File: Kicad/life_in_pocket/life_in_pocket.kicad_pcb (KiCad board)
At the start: 2 copper layers, 115.7 x 79.1 mm, 57 parts, among them J2 USB_C_Receptacle_USB2.0_16P, Q1 QM6015D, SW1 SW_SPST, SW2 Switch, SW3 Switch, SW4 Switch, SW5 Switch, U1 ESP32-S3-WROOM-1, U2 Adafruit I2S 3W Class D Ampli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, U3 MicroSd breakout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

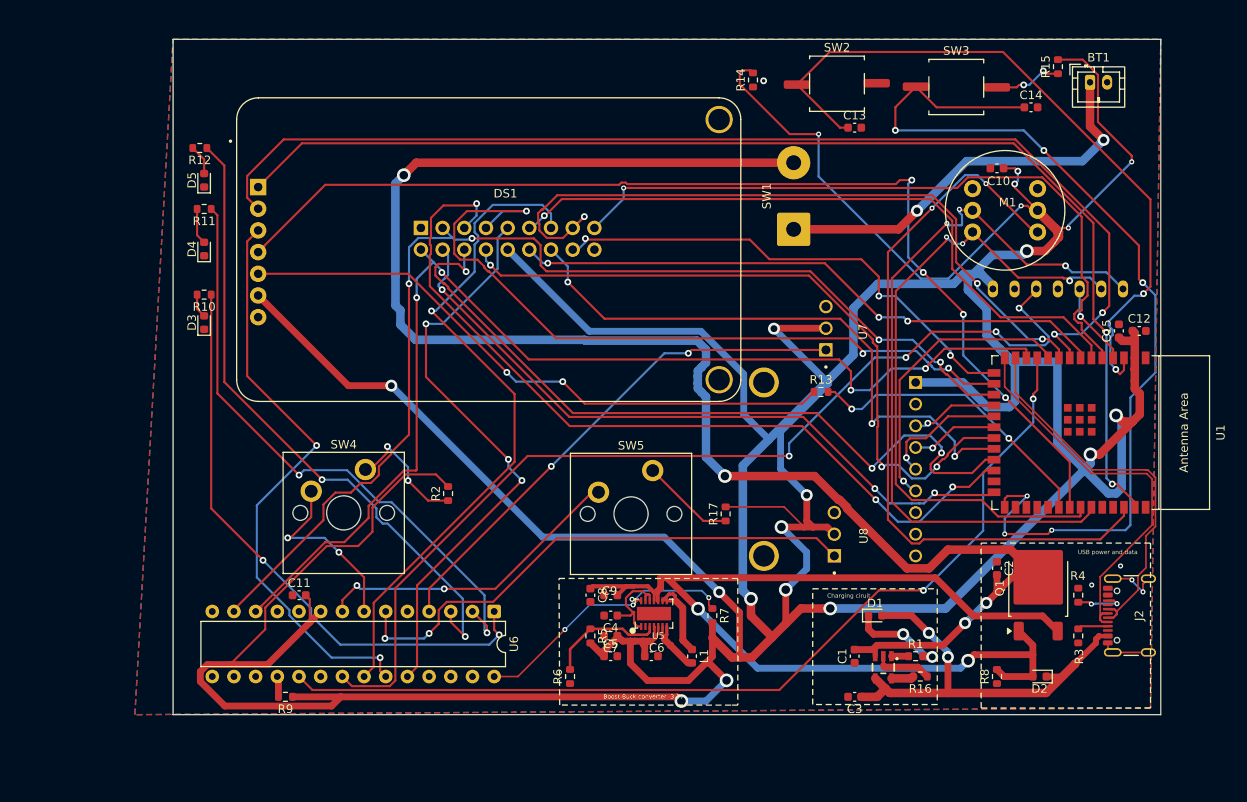
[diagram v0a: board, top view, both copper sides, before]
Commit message: Finished rerouting- all critical errors resolved
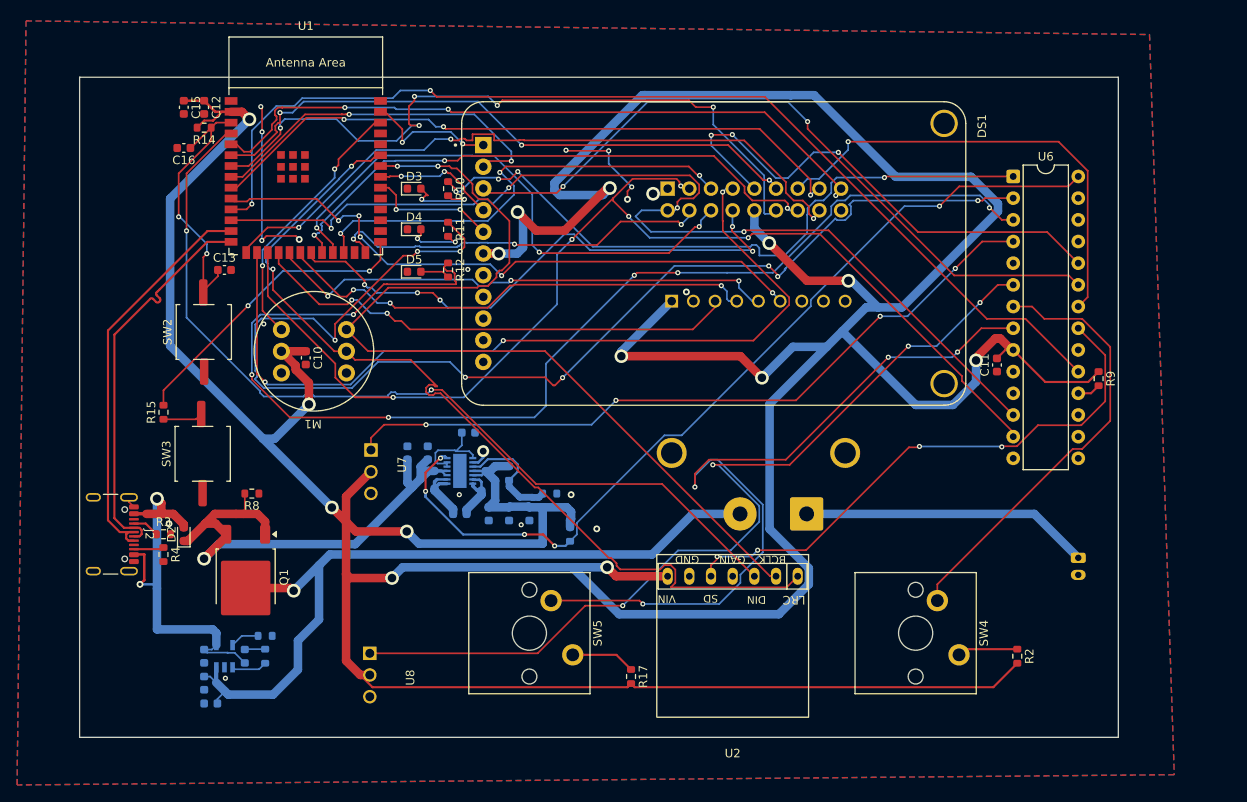
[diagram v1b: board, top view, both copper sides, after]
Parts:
- removed C14: 0.1uF, Capacitor_SMD:C_0603_1608Metric
- removed R13: 33, Resistor_SMD:R_0603_1608Metric
- added C16: 1.0uF, Capacitor_SMD:C_0603_1608Metric, F.Cu at (97.6, 52.4)
- BT1, C1, C2, C3, C4, C5, C6, C7, C8, C9, D1, L1, R1, R16, R5, R6, R7, SW1, U4, U5: moved to B.Cu
- R15: value 10k -> 100
- U2: moved to F.Cu
- moved J2 121.8 mm to (88.1, 97.6), turned to -90 degrees
- moved C12 112.6 mm to (100.0, 47.6), turned to -90 degrees
- moved C15 112.6 mm to (97.6, 47.6), turned to -90 degrees
- moved R15 112.3 mm to (95.2, 83.3)
- moved R3 107.8 mm to (95.2, 97.6), turned to 0 degrees
- moved R4 107.3 mm to (95.2, 100.0), turned to -90 degrees
- moved R9 102.3 mm to (204.8, 79.4), turned to -90 degrees
- moved D2 101.6 mm to (97.6, 97.6), turned to 90 degrees
- moved SW3 98.2 mm to (99.8, 88.2), turned to -90 degrees
- moved U1 95.2 mm to (111.9, 55.1), turned to 0 degrees
- moved C2 93.4 mm to (100.8, 117.5), turned to 0 degrees
- moved Q1 92.8 mm to (104.9, 102.7), turned to -90 degrees
- moved R8 89.9 mm to (105.6, 92.9), turned to 180 degrees
- moved C11 86.1 mm to (192.9, 77.8), turned to 90 degrees
- moved C10 84.0 mm to (111.9, 77.0), turned to -90 degrees
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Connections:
- C13 pad 1: 3.3V -> EN
- C4 pad 1: Net-(U5-EN) -> GND
- C4 pad 2: GND -> Net-(U5-EN)
- C8 pad 1: Net-(D2-A) -> Net-(D2-K)
- C9 pad 1: Net-(D2-A) -> Net-(D2-K)
- D2 pad 1: VBUS -> Net-(D2-K)
- D2 pad 2: Net-(D2-A) -> VBUS
- Q1 pad 1: Net-(D2-A) -> Net-(D2-K)
- Q1 pad 3: Net-(D2-A) -> Net-(D2-K)
- R14 pad 1: GND -> EN
- R15 pad 1: GND -> Net-(R15-Pad1)
- R15 pad 2: 3.3V -> BOOT
- R8 pad 2: Net-(D2-A) -> Net-(D2-K)
- SW2 pad 1: 3.3V -> EN
- SW3 pad 1: 3.3V -> Net-(R15-Pad1)
- U1 pad 27: 3.3V -> BOOT
- U1 pad 3: 3.3V -> EN
- U1 pad 32: Net-(U1-MTCK/GPIO39/CLK_OUT3/SUBSPICS1) -> TFT_SCL
- U5 pad P10: Net-(D2-A) -> Net-(D2-K)
- U5 pad P11: Net-(D2-A) -> Net-(D2-K)
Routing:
- net 3.3V: track 870.0 -> 570.0 mm, vias 27 -> 14
- net TFT_CS: track 139.4 -> 15.7 mm
- net Net-(D2-A): track 121.9 -> 0.00 mm, vias 2 -> 0
- net TFT_SDA: track 126.6 -> 14.4 mm, vias 4 -> 2
- net BAT+: track 189.6 -> 91.7 mm, vias 4 -> 1
- net AMP_DIN: track 9.70 -> 104.3 mm, vias 1 -> 2
- net TFT_DC: track 131.5 -> 42.3 mm
- net Net-(U6-GPB1): track 71.2 -> 145.0 mm, vias 2 -> 8
- net GPA7: track 32.8 -> 104.5 mm, vias 4 -> 5
- net Net-(U6-GPB2): track 75.5 -> 142.6 mm, vias 2 -> 6
- net Net-(D2-K): track 0.00 -> 62.3 mm, vias 0 -> 1
- net TFT_SCL: track 72.0 -> 15.2 mm
- net MIC_SD: track 86.7 -> 31.3 mm
- net Net-(U6-GPB7): track 36.9 -> 91.8 mm, vias 2 -> 4
- net AMP_SD: track 117.0 -> 65.5 mm
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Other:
- board size 115.7 x 79.1 mm -> 121.7 x 77.3 mm
- board text removed: "Boost-Buck converter -3.3v"
- board text removed: "Charging ciruit"
- board text removed: "USB power and data"

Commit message: Kicad stuff done. began firmware setup
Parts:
- added H1: MountingHole_Pad, MountingHole:MountingHole_3.2mm_M3_DIN965_Pad_TopBottom, F.Cu at (90.5, 50.0)
- added H2: MountingHole_Pad, MountingHole:MountingHole_3.2mm_M3_DIN965_Pad_TopBottom, F.Cu at (202.4, 50.0)
- added H3: MountingHole_Pad, MountingHole:MountingHole_3.2mm_M3_DIN965_Pad_TopBottom, F.Cu at (202.4, 116.7)
- added H4: MountingHole_Pad, MountingHole:MountingHole_3.2mm_M3_DIN965_Pad_TopBottom, F.Cu at (90.5, 116.7)
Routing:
- net GND: track 36.1 -> 39.1 mm
- net 3.3V: track 570.0 -> 571.6 mm
- net D5: track 80.2 -> 80.9 mm
- net D1: track 67.0 -> 67.6 mm
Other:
- outline, holes or cut-outs redrawn
